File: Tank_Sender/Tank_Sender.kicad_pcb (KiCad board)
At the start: 2 copper layers, 19.5 x 16 mm, 12 parts, among them J101 Interface, J102 TANK, J103 TANK, U101 H7550-H#

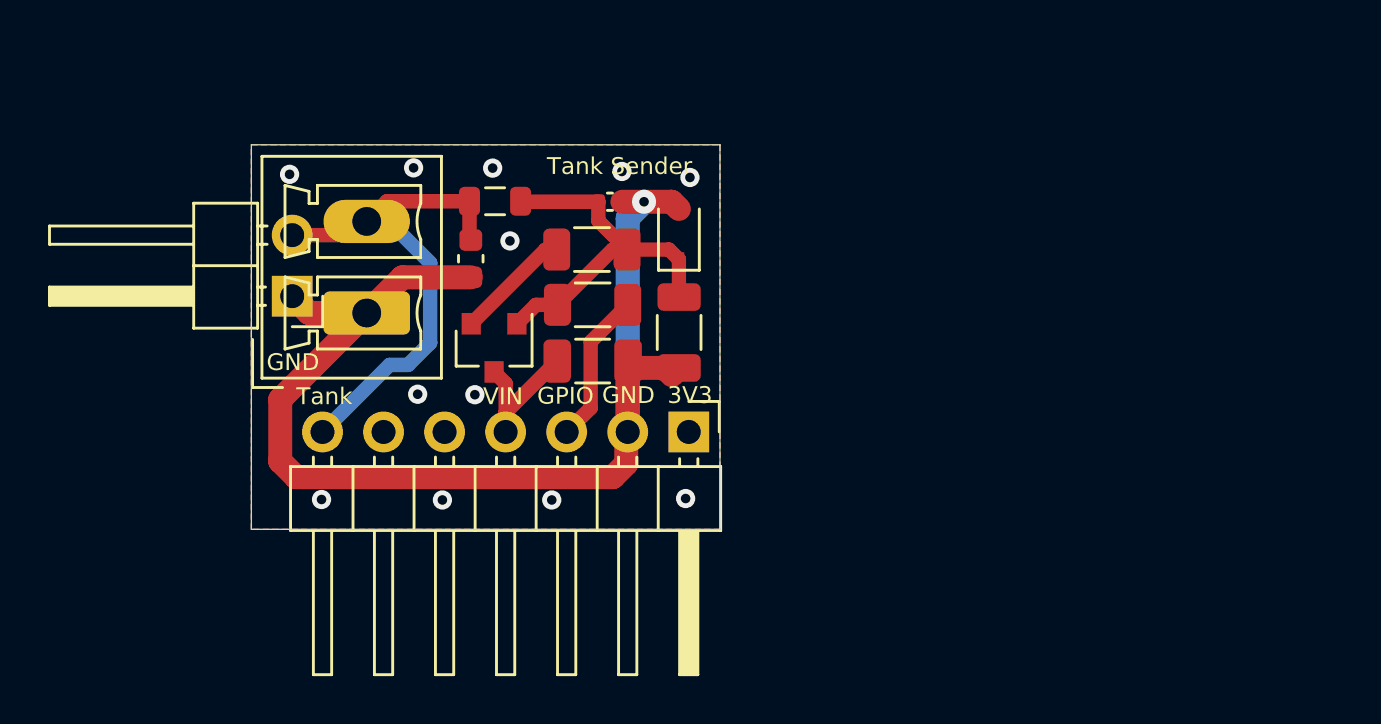
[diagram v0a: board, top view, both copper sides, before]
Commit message: Standardize on 20mm x 20mm boards with 7pin header
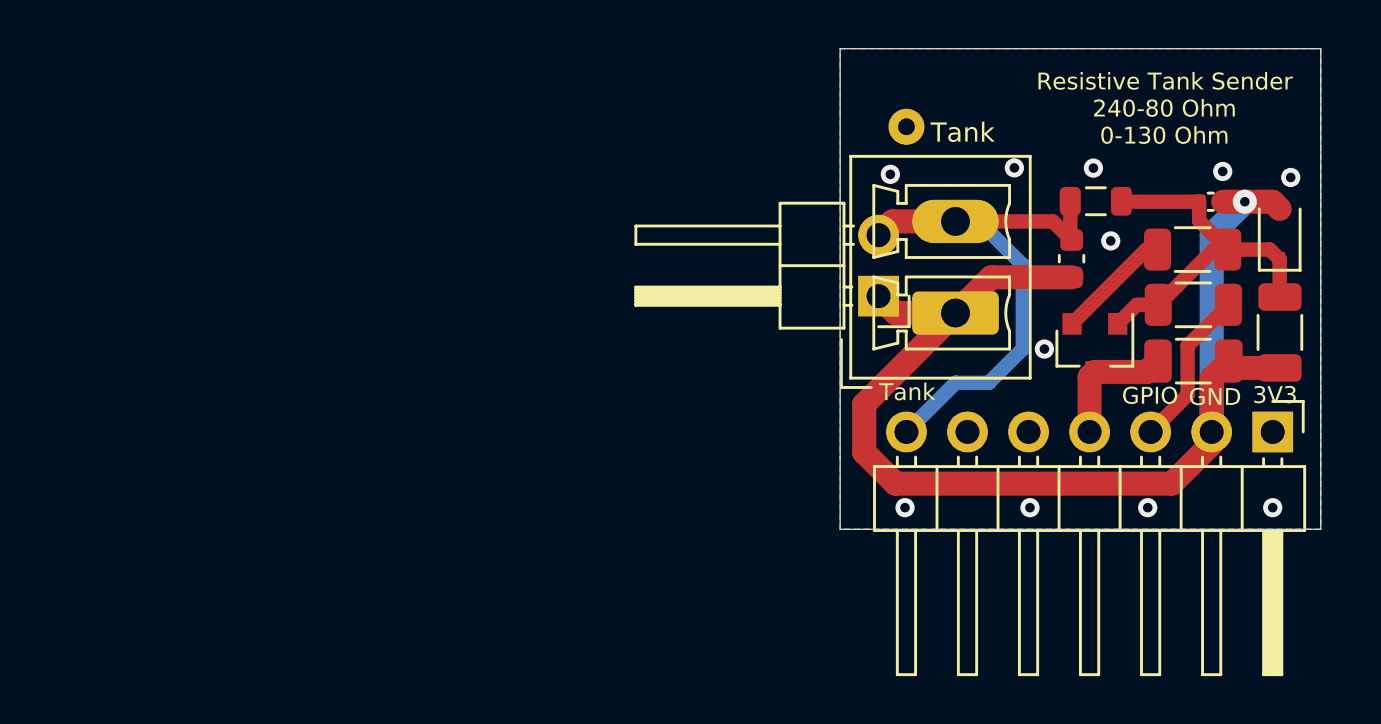
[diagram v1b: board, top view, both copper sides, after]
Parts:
- added REF**: TestPoint_THTPad_D1.5mm_Drill0.7mm, TestPoint:TestPoint_THTPad_D1.5mm_Drill0.7mm, F.Cu at (147.8, 76.2)
- moved C101 25.0 mm to (159.7, 86.0)
- moved C102 25.0 mm to (163.3, 84.8)
- moved C103 25.0 mm to (160.4, 79.4)
- moved C104 25.0 mm to (154.6, 81.7)
- moved D101 25.0 mm to (163.3, 80.7)
- moved FB101 25.0 mm to (155.6, 79.3)
- moved R101 25.0 mm to (159.7, 83.7)
- moved R102 25.0 mm to (159.7, 81.4)
- moved U101 25.0 mm to (155.6, 85.5)
- moved J103 24.5 mm to (149.8, 84.0)
- moved J102 24.4 mm to (146.6, 83.3)
- moved J101 24.3 mm to (163.0, 89.0)
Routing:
- net /Tank: track 23.6 -> 26.0 mm
- net GND: track 50.2 -> 51.3 mm, vias 13 -> 12
- net /VIN_PROT: track 6.54 -> 5.40 mm
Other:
- board size 19.5 x 16 mm -> 20 x 20 mm
- board text added: "Hole here is for Single pin to support board edge if needed for connectors when Horizontal on SH-ESP32"
- board text added: "Resistive Tank Sender 240-80 Ohm 0-130 Ohm"
- board text removed: "240-80 Ohm 0-130 Ohm Tank Sender"
- board text removed: "Leave Free if extending board raise bottom edge 4mm to clear components on SH-ESP32"
- board text removed: "Tank Sender"
- board text removed: "VIN"
- board text removed: "VIN +12V"

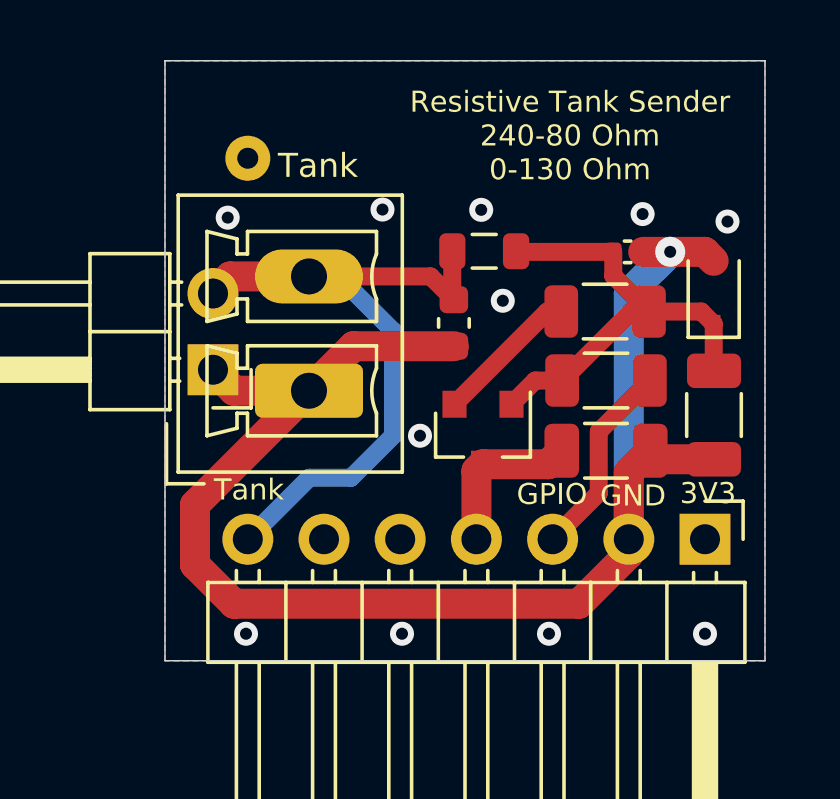
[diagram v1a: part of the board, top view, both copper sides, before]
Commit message: New GND Pin.  Added PI Filters to all inputs.    Refined Layout
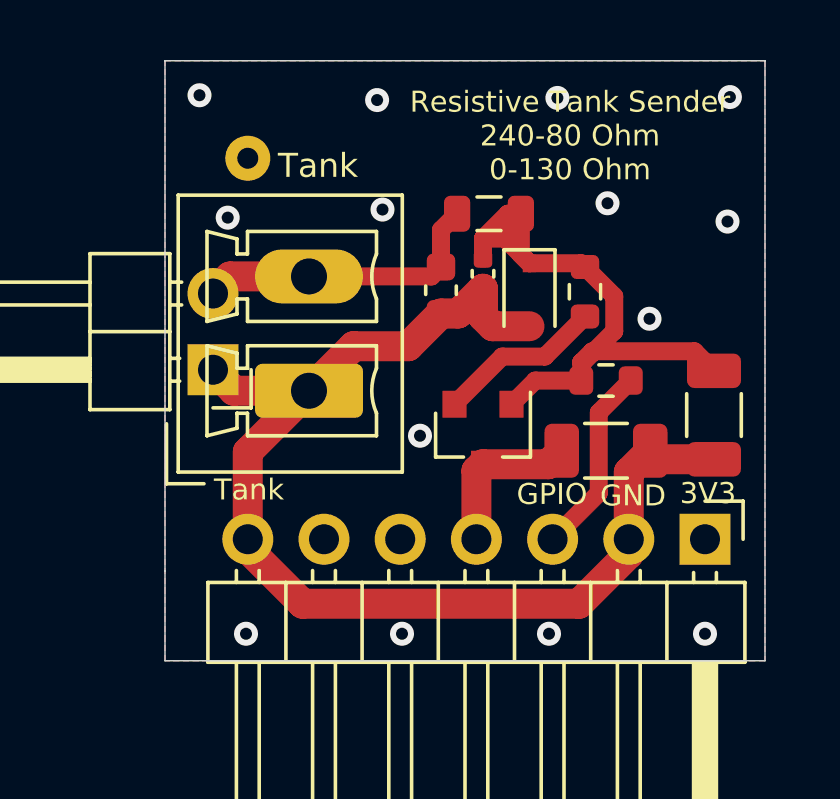
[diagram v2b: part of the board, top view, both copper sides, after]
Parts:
- R101, R102: footprint Resistor_SMD:R_1206_3216Metric -> Resistor_SMD:R_0603_1608Metric
- moved D101 6.14 mm to (157.2, 80.8), turned to 270 degrees
- moved C103 4.87 mm to (155.6, 80.1), turned to 270 degrees
- moved FB101 1.26 mm to (155.8, 78.1)
- moved C104 1.17 mm to (154.2, 80.7)
- moved R102 0.94 mm to (159.0, 80.7), turned to 90 degrees
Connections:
- J101 pad 7: /Tank -> GND
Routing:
- net /Tank: track 26.0 -> 13.1 mm
- net GND: track 51.3 -> 39.6 mm, vias 12 -> 14
- net Net-(C102-Pad1): track 15.5 -> 21.1 mm
- net Net-(R102-Pad1): track 4.84 -> 5.56 mm

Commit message: Opto - LCSC Parts added
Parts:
- D101: value MM2Z70 -> KDZ3.3V-RTK/P
